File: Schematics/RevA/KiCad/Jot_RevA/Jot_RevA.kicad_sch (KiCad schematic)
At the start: 0 parts

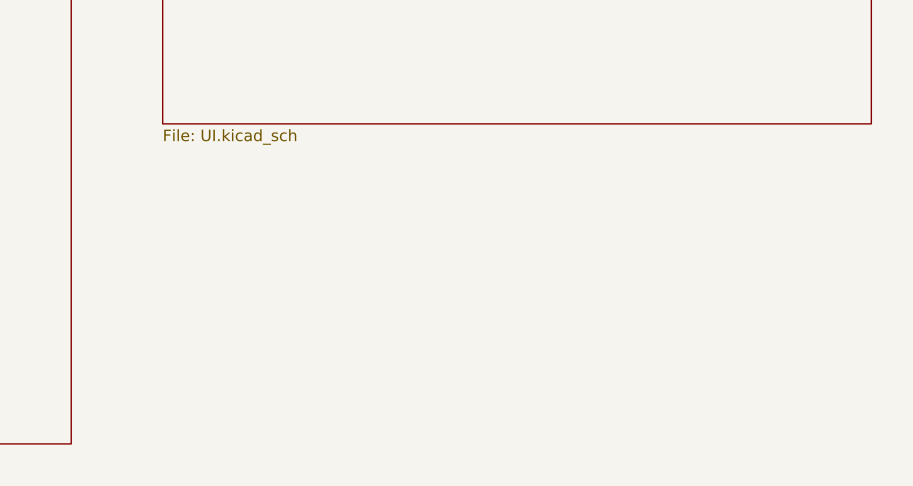
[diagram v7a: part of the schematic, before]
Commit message: Debug sheet: TP3-TP9 test pads for SWDIO, SWDCLK, nRESET, +3V3, GND, UART_TX, UART_RX; UI sheet re-laid out (nets unchanged)
Co-Authored-By: Claude Opus 5.5 <noreply@anthropic.com>
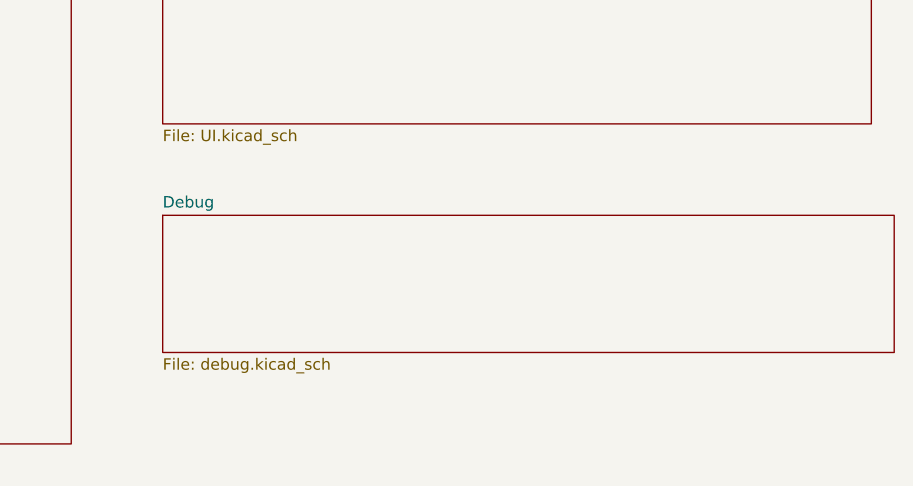
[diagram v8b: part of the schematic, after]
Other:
- added sheet Debug (debug.kicad_sch)
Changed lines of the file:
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@@
+		)
+	)
+	(sheet
+		(at 203.2 129.54)
+		(size 81.28 15.24)
+		(exclude_from_sim no)
+		(in_bom yes)
+		(on_board yes)
+		(dnp no)
+		(fields_autoplaced yes)
+		(stroke
+			(width 0.1524)
+			(type solid)
+		)
+		(fill
+			(color 0 0 0 0)
+		)
+		(property "Sheetname" "Debug"
+			(at 203.2 128.8284 0)
+			(show_name no)
+			(do_not_autoplace no)
+			(effects
+				(font
+					(size 1.27 1.27)
+				)
+				(justify left bottom)
+			)
+		)
+		(property "Sheetfile" "debug.kicad_sch"
+			(at 203.2 145.3646 0)
+			(show_name no)
+			(do_not_autoplace no)
+			(effects
+				(font
+					(size 1.27 1.27)
+				)
+				(justify left top)
+			)
+		)
+		(instances
+			(project "Jot_RevA"
+				(path "/61747270-9f90-47b6-9c50-5ea1f41f259a"
+					(page "8")
+				)
+			)
 		)
 	)
